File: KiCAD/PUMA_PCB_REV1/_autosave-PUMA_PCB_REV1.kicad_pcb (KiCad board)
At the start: 4 copper layers, 141.7 x 141.5 mm, 49 parts, among them J1 SAMTEC-TMM-116-01-X-D-SM, U1 MICROFC-30035-SMT-TR1, U10 MICROFC-30035-SMT-TR1, U11 MICROFC-30035-SMT-TR1, U12 MICROFC-30035-SMT-TR1, U13 MICROFC-30035-SMT-TR1, U14 MICROFC-30035-SMT-TR1, U15 MICROFC-30035-SMT-TR1, U16 MICROFC-30035-SMT-TR1, U2 MICROFC-30035-SMT-TR1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

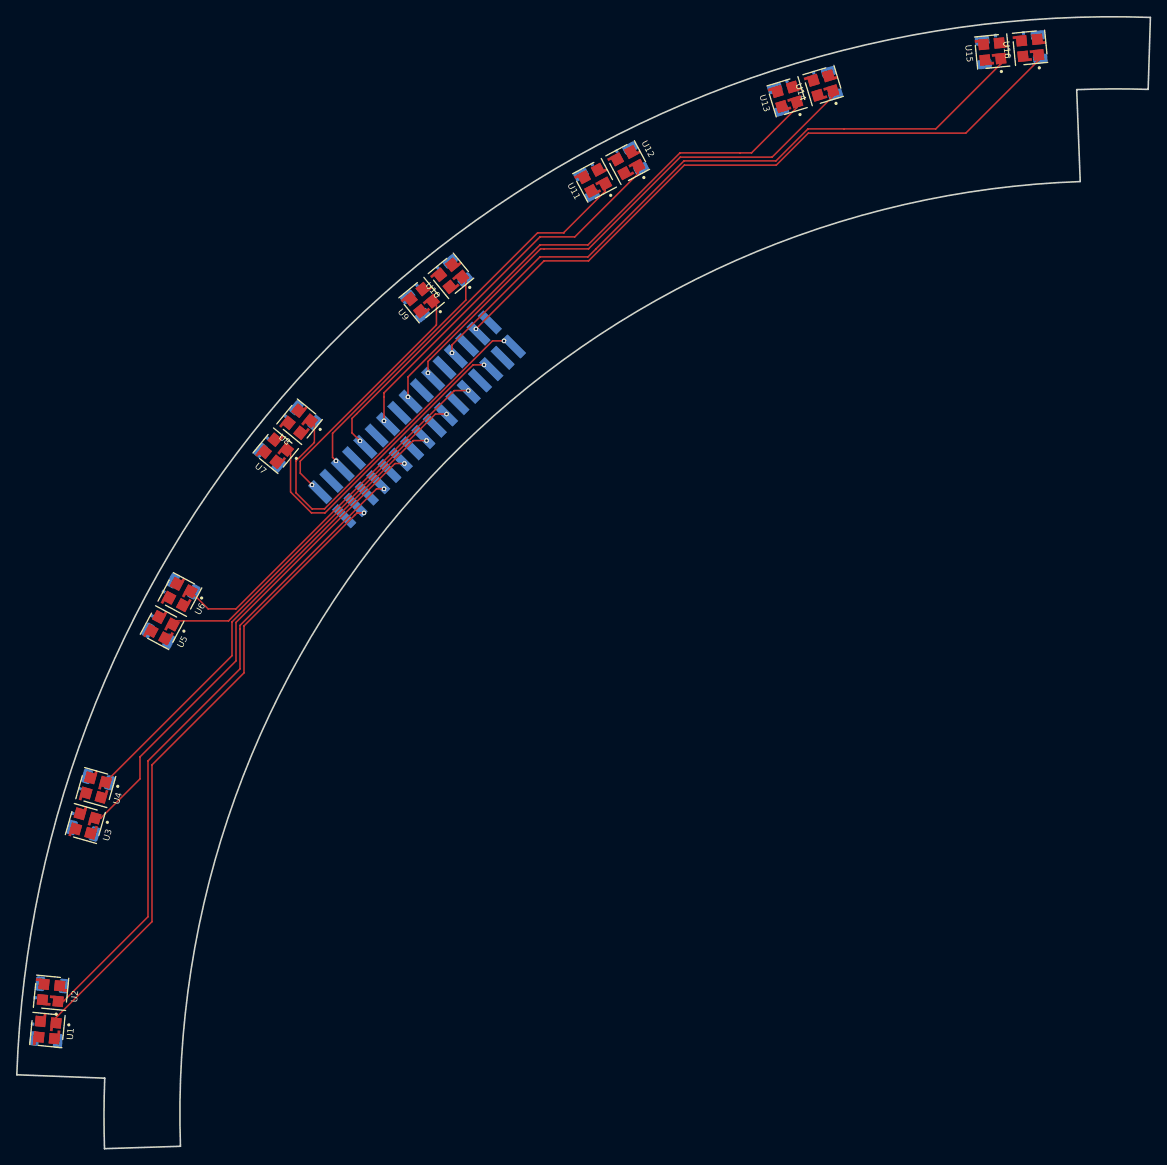
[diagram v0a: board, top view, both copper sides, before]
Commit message: traces and vias for first group of SiPMs
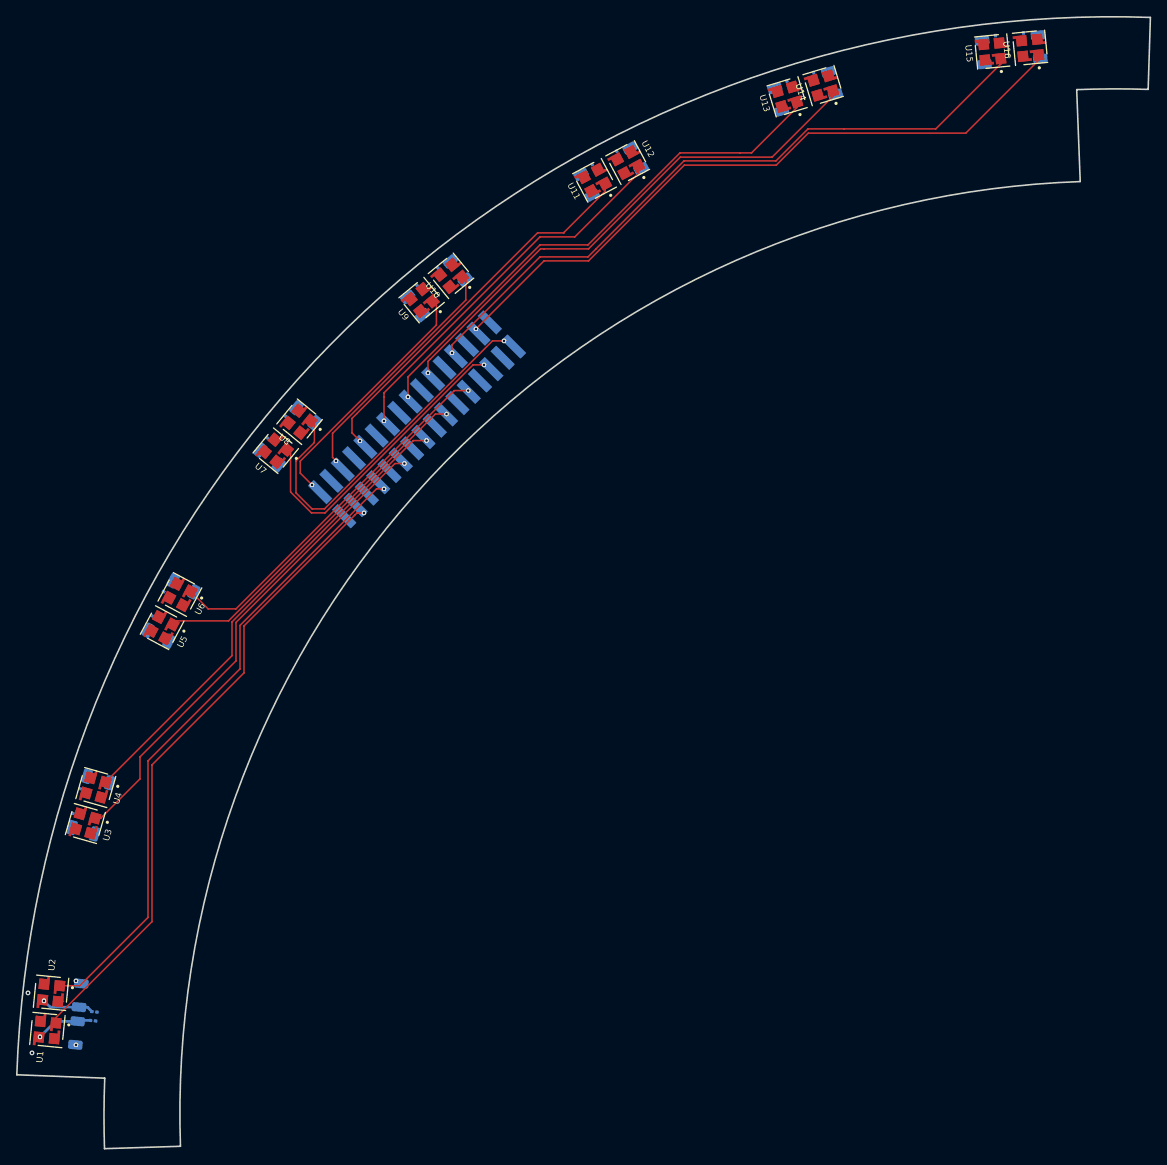
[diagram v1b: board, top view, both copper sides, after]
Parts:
- moved R2 7.28 mm to (61.4, 156.7)
- moved R1 7.25 mm to (61.2, 157.8), turned to 174.35 degrees
- moved C1 3.88 mm to (59.1, 159.4), turned to -95.65 degrees
- moved C2 3.76 mm to (59.6, 154.7), turned to 84.351 degrees
- turned U2 to 174.4 degrees
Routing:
- net Net-(C1-Pad1): track 0.00 -> 6.95 mm, vias 0 -> 1
- net Net-(C2-Pad1): track 0.00 -> 6.54 mm, vias 0 -> 1
- net PW_2: track 81.9 -> 80.9 mm
- net unconnected-(U2-Pad4): track 0.00 -> 0.66 mm
- net GND: vias 0 -> 2
- net (no net): vias 0 -> 2
